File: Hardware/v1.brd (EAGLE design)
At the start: 50 x 40 mm, 75 parts, among them IC1 LM324D, IC2 m328p, IC3 REG1117, J1 22-27-2061-06, J2 22-27-2021-02, J3 22-27-2021-02, J4 22-27-2031-03, J5 22-27-2041-04, Q1 BSS123, Q2 BSS123, Q3 BSS123, Q5 BSS123

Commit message: slight changes in the layout
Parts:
- C9: value (none) -> 1000u
- L1, L2: device rcl:L2012C -> rcl:L2825P
- U$1: device IRF7424:SO-08 -> MyLib:SO-08
- U$3: value ELKO-1,27-4,2 -> 330u; device MyLib:ELKO-1,27-4,5 -> rcl:E2-5
- U$4: value ELKO-1,27-4,2 -> 330u; device MyLib:ELKO-1,27-4,5 -> rcl:E3,5-8
- moved TP12 2.29 mm to (9.08, 35.6), flipped to the bottom
- moved U$4 2.10 mm to (11.2, 35.7)
- moved C5 1.40 mm to (23.0, 2.71), turned to 90 degrees
- moved TP8 1.11 mm to (9.08, 37.8)
- moved L2 0.95 mm to (15.3, 33.8)
- moved U$3 0.94 mm to (2.98, 28.5), turned to 90 degrees
- moved L1 0.59 mm to (19.7, 2.58)
- moved R24 0.51 mm to (12.1, 31.6)
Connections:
- net 12V: now also U$4.+; no longer U$4.P$1
- net GND: now also U$3.-, U$4.-; no longer U$3.P$2, U$4.P$2
- net VCC: now also U$3.+; no longer U$3.P$1
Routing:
- net VCC: track 148.6 -> 145.7 mm
- net N$26: track 5.80 -> 8.57 mm
- net N$5: track 4.79 -> 7.38 mm
- net N$3: track 3.33 -> 5.04 mm
- net 12V: track 82.1 -> 80.8 mm

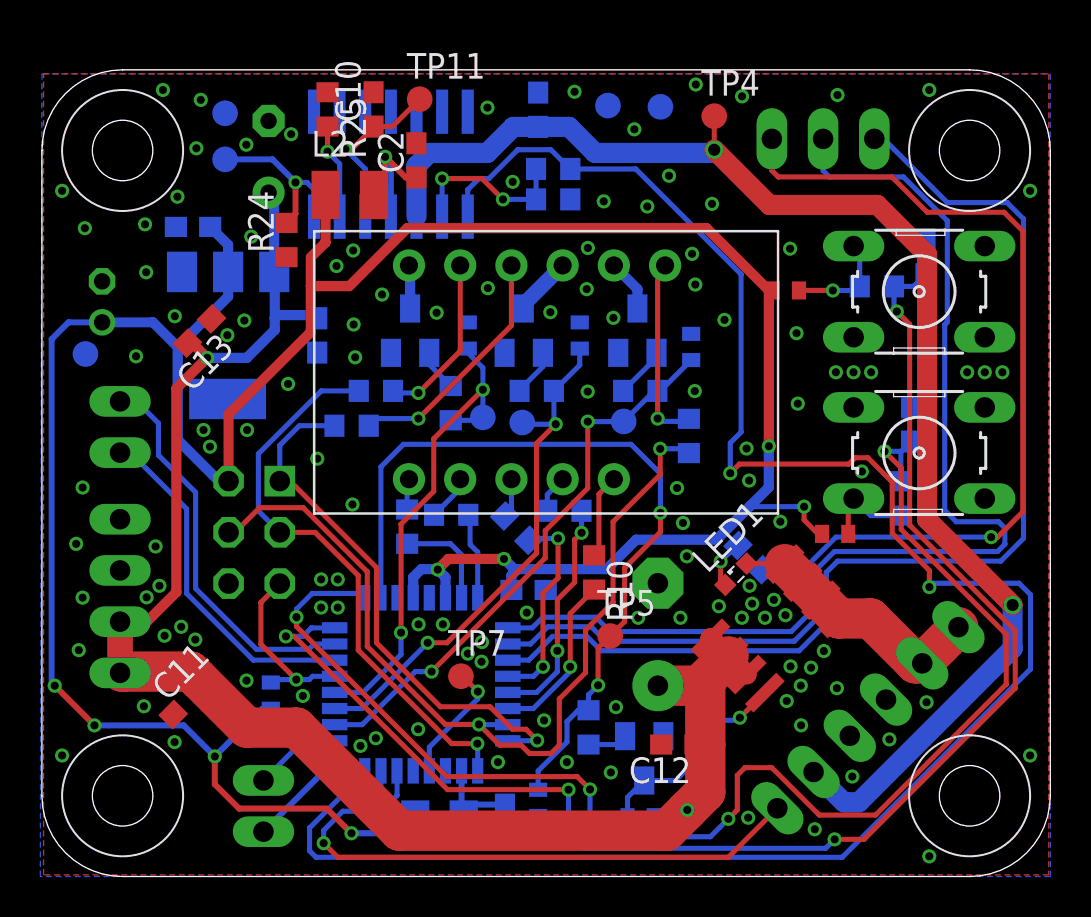
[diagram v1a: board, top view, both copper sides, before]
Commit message: finish layer done so pcb will have the components names printed on it
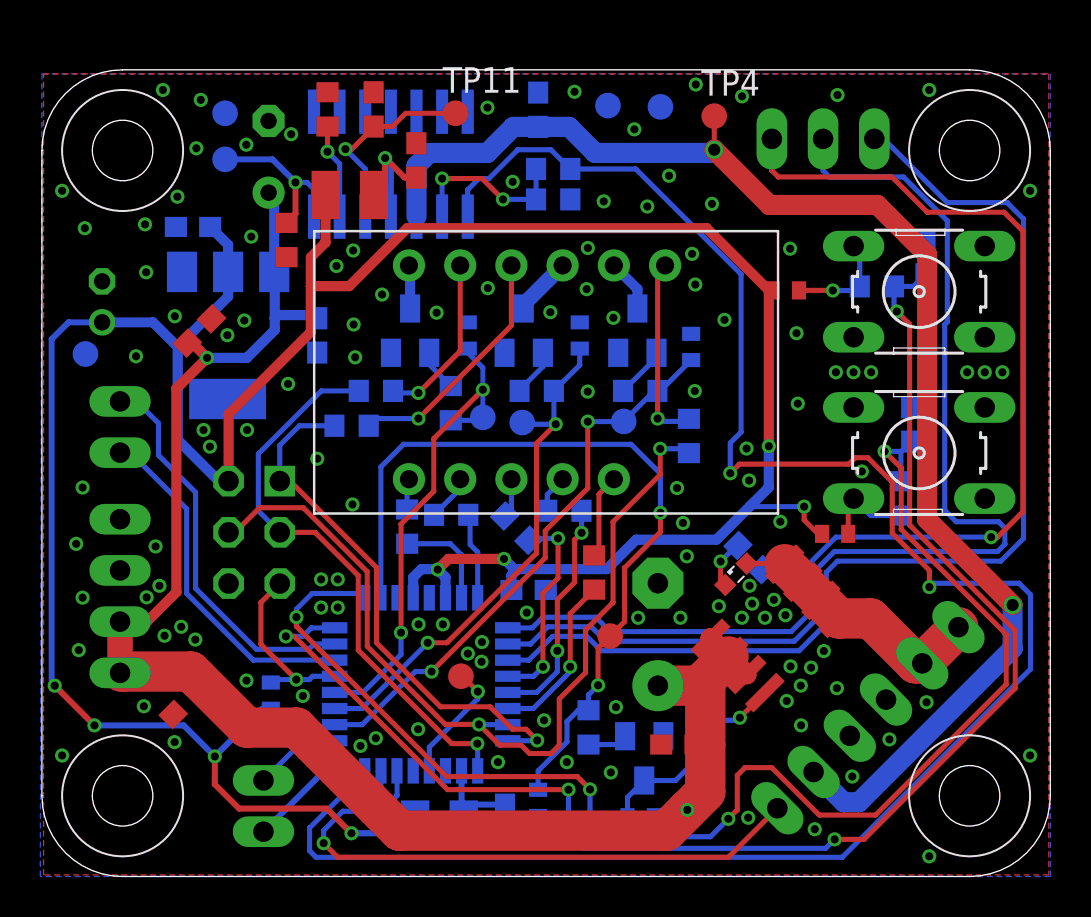
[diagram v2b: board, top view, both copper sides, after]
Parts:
- moved TP11 1.91 mm to (20.5, 37.8)
- renumbered U$3 to C15, U$4 to C14
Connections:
- net N$27 renamed ADC7
- net N$28 renamed ADC1
- net N$29 renamed ADC2
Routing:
- net N$30: track 8.49 -> 9.97 mm
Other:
- board text removed: "ADC6"
- board text removed: "ADC7"
- board text removed: "by JB v1.0 08-2014"

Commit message: op-amp rework
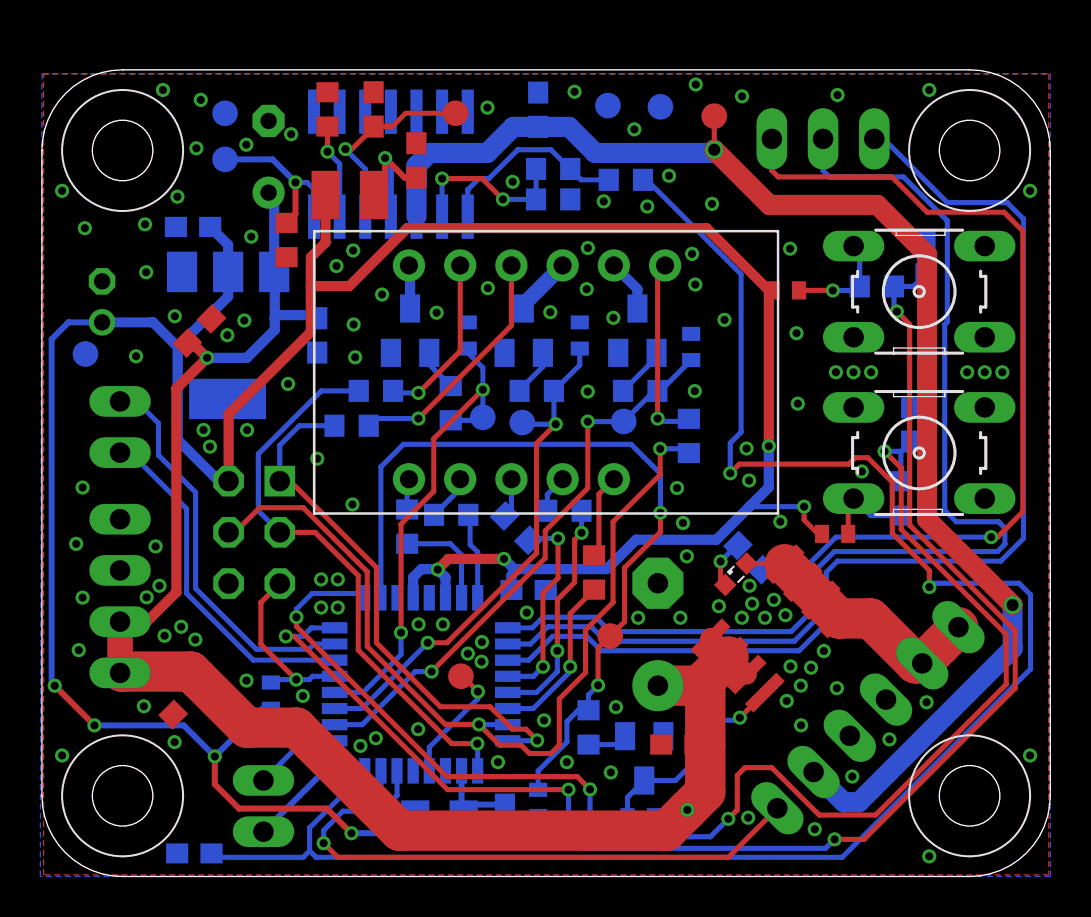
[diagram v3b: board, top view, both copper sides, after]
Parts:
- added C16: 10n, rcl:C0603
- added R27: 5k6, rcl:R0603
- R1: value 750k -> 68k
- R2: value 1k2 -> 100
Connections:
- new net SDFGHJK: IC1.1, R1.2, R27.1
- net ADC0: now also C16.1, R27.2; no longer IC1.1, R1.2
- net GND: now also C16.2
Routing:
- net SDFGHJK: track 0.00 -> 9.76 mm
- net ADC0: track 98.3 -> 91.9 mm
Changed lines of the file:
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@@
 <layer number="23" name="tOrigins" color="15" fill="1" visible="yes" active="yes"/>
 <layer number="24" name="bOrigins" color="15" fill="1" visible="yes" active="yes"/>
-<layer number="25" name="tNames" color="7" fill="1" visible="no" active="yes"/>
-<layer number="26" name="bNames" color="7" fill="1" visible="no" active="yes"/>
-<layer number="27" name="tValues" color="7" fill="1" visible="no" active="yes"/>
-<layer number="28" name="bValues" color="7" fill="1" visible="no" active="yes"/>
+<layer number="25" name="tNames" color="7" fill="1" visible="yes" active="yes"/>
+<layer number="26" name="bNames" color="7" fill="1" visible="yes" active="yes"/>
+<layer number="27" name="tValues" color="7" fill="1" visible="yes" active="yes"/>
+<layer number="28" name="bValues" color="7" fill="1" visible="yes" active="yes"/>
 <layer number="29" name="tStop" color="7" fill="3" visible="yes" active="yes"/>
 <layer number="30" name="bStop" color="7" fill="6" visible="yes" active="yes"/>
@@
 <elements>
 <element name="IC1" library="linear" package="SO14" value="LM324D" x="17.30375" y="35.321875" smashed="yes" rot="MR0"/>
-<element name="R2" library="rcl" package="R0603" value="1k2" x="25.352375" y="33.575625" smashed="yes" rot="MR0">
-<attribute name="NAME" x="26.781125" y="34.178875" size="1.143" layer="34" font="vector" ratio="15" rot="MR180"/>
-</element>
-<element name="R1" library="rcl" package="R0603" value="750k" x="25.352375" y="35.08375" smashed="yes" rot="MR180">
-<attribute name="NAME" x="26.749375" y="35.71875" size="1.143" layer="34" font="vector" ratio="15" rot="MR180"/>
+<element name="R2" library="rcl" package="R0603" value="100" x="25.352375" y="33.575625" smashed="yes" rot="MR0">
+<attribute name="NAME" x="24.114125" y="32.718375" size="1.143" layer="34" font="vector" ratio="15" rot="MR180"/>
+</element>
+<element name="R1" library="rcl" package="R0603" value="68k" x="25.352375" y="35.08375" smashed="yes" rot="MR180">
+<attribute name="NAME" x="26.622375" y="36.41725" size="1.143" layer="34" font="vector" ratio="15" rot="MR180"/>
 </element>
 <element name="C1" library="rcl" package="C0603" value="10n" x="24.60625" y="38.020625" smashed="yes" rot="MR90">
@@
 <attribute name="VALUE" x="29.48305" y="21.802725" size="0.0254" layer="28" rot="MR0"/>
 </element>
-<element name="TP4" library="testpad" package="B1,27" value="PTR1B1,27" x="33.3375" y="37.703125">
-<attribute name="TP_SIGNAL_NAME" value="" x="33.3375" y="37.703125" size="1.778" layer="27" display="off"/>
+<element name="TP4" library="testpad" package="B1,27" value="PTR1B1,27" x="33.3375" y="37.703125" smashed="yes">
+<attribute name="TP_SIGNAL_NAME" value="" x="32.7025" y="35.798125" size="1" layer="37"/>
+<attribute name="VALUE" x="32.7025" y="36.941125" size="0.0254" layer="27"/>
 </element>
 <element name="TP5" library="testpad" package="B1,27" value="PTR1B1,27" x="28.178125" y="11.922125" smashed="yes">
@@
 <attribute name="NAME" x="17.3355" y="38.608" size="1.143" layer="33" font="vector" ratio="15"/>
 </element>
-<element name="TP11" library="testpad" package="B1,27" value="PTR1B1,27" x="20.5105" y="37.846">
-<attribute name="TP_SIGNAL_NAME" value="" x="20.5105" y="37.846" size="1.778" layer="27" display="off"/>
+<element name="TP11" library="testpad" package="B1,27" value="PTR1B1,27" x="20.5105" y="37.846" smashed="yes">
+<attribute name="TP_SIGNAL_NAME" value="" x="19.8755" y="35.941" size="1" layer="37"/>
+<attribute name="VALUE" x="19.8755" y="37.084" size="0.0254" layer="27"/>
 </element>
 <element name="TP12" library="testpad" package="B1,27" value="PTR1B1,27" x="9.0805" y="35.56" smashed="yes" rot="MR0">
@@
 <element name="C14" library="rcl" package="E3,5-8" value="330u" x="11.2395" y="35.687" smashed="yes" rot="MR90">
 <attribute name="NAME" x="12.954" y="35.1155" size="1.143" layer="34" font="vector" ratio="15" rot="MR0"/>
+</element>
+<element name="C16" library="rcl" package="C0603" value="10n" x="7.5565" y="1.143" smashed="yes" rot="MR0">
+<attribute name="NAME" x="8.89" y="2.032" size="1.143" layer="34" font="vector" ratio="15" rot="MR0"/>
+</element>
+<element name="R27" library="rcl" package="R0603" value="5k6" x="28.956" y="34.544" smashed="yes" rot="MR180">
+<attribute name="NAME" x="28.702" y="33.655" size="1.143" layer="34" font="vector" ratio="15" rot="MR180"/>
 </element>
 </elements>
@@
 <via x="13.843" y="14.732" extent="1-16" drill="0.4"/>
 <via x="14.6685" y="14.732" extent="1-16" drill="0.4"/>
+<contactref element="C16" pad="2"/>
 </signal>
 <signal name="N$1">
@@
 <signal name="ADC0">
 <contactref element="IC2" pad="23"/>
-<wire x1="29.448125" y1="35.08375" x2="34.671" y2="29.860875" width="0.254" layer="16"/>
 <wire x1="16.80875" y1="4.346875" x2="16.80875" y2="5.235525" width="0.254" layer="16"/>
-<contactref element="IC1" pad="1"/>
-<contactref element="R1" pad="2"/>
-<wire x1="25.24125" y1="36.03625" x2="26.19375" y2="35.08375" width="0.254" layer="16"/>
-<wire x1="26.19375" y1="35.08375" x2="26.202375" y2="35.08375" width="0.254" layer="16"/>
-<wire x1="29.448125" y1="35.08375" x2="26.202375" y2="35.08375" width="0.254" layer="16"/>
-<wire x1="21.11375" y1="34.051875" x2="21.11375" y2="32.721875" width="0.254" layer="16"/>
 <wire x1="16.80875" y1="4.346875" x2="16.589375" y2="4.1275" width="0.254" layer="16"/>
 <wire x1="16.589375" y1="4.1275" x2="14.986" y2="4.1275" width="0.254" layer="16"/>
@@
 <wire x1="40.005" y1="20.447" x2="34.5821" y2="20.447" width="0.254" layer="1"/>
 <wire x1="44.196" y1="14.5415" x2="44.0055" y2="14.351" width="0.254" layer="16"/>
-<wire x1="21.11375" y1="34.051875" x2="21.669375" y2="34.6075" width="0.254" layer="16"/>
-<wire x1="21.669375" y1="34.6075" x2="22.1615" y2="34.6075" width="0.254" layer="16"/>
-<wire x1="22.1615" y1="34.6075" x2="23.59025" y2="36.03625" width="0.254" layer="16"/>
-<wire x1="23.59025" y1="36.03625" x2="25.24125" y2="36.03625" width="0.254" layer="16"/>
+<contactref element="C16" pad="1"/>
+<contactref element="R27" pad="2"/>
+<wire x1="34.671" y1="29.860875" x2="29.987875" y2="34.544" width="0.25" layer="16"/>
+<wire x1="29.987875" y1="34.544" x2="29.806" y2="34.544" width="0.25" layer="16"/>
+<wire x1="8.4065" y1="1.143" x2="8.509" y2="1.143" width="0.25" layer="16"/>
+<wire x1="8.509" y1="1.143" x2="8.6995" y2="0.9525" width="0.25" layer="16"/>
+<wire x1="8.6995" y1="0.9525" x2="12.954" y2="0.9525" width="0.25" layer="16"/>
+<wire x1="12.954" y1="0.9525" x2="13.2715" y2="1.27" width="0.25" layer="16"/>
 </signal>
 <signal name="SENSOR0">
@@
 <wire x1="18.034" y1="37.846" x2="17.3745" y2="37.1865" width="0.25" layer="1"/>
 </signal>
+<signal name="SDFGHJK">
+<contactref element="IC1" pad="1"/>
+<contactref element="R1" pad="2"/>
+<contactref element="R27" pad="1"/>
+<wire x1="25.24125" y1="36.03625" x2="26.19375" y2="35.08375" width="0.254" layer="16"/>
+<wire x1="26.19375" y1="35.08375" x2="26.202375" y2="35.08375" width="0.254" layer="16"/>
+<wire x1="21.11375" y1="34.051875" x2="21.11375" y2="32.721875" width="0.254" layer="16"/>
+<wire x1="21.11375" y1="34.051875" x2="21.669375" y2="34.6075" width="0.254" layer="16"/>
+<wire x1="21.669375" y1="34.6075" x2="22.1615" y2="34.6075" width="0.254" layer="16"/>
+<wire x1="22.1615" y1="34.6075" x2="23.59025" y2="36.03625" width="0.254" layer="16"/>
+<wire x1="23.59025" y1="36.03625" x2="25.24125" y2="36.03625" width="0.254" layer="16"/>
+<wire x1="26.202375" y1="35.08375" x2="26.742125" y2="34.544" width="0.25" layer="16"/>
+<wire x1="26.742125" y1="34.544" x2="28.106" y2="34.544" width="0.25" layer="16"/>
+</signal>
 </signals>

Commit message: latest version with some updates
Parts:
- added AREF: PTR1B1,27, testpad:B1,27
- R1: value 68k -> 43k
- moved TP7 9.94 mm to (11.4, 6.73), flipped to the bottom
- moved R15 0.54 mm to (33.1, 7.28)
- moved TP4 0.51 mm to (32.8, 37.8)
- moved C6 0.45 mm to (7.81, 31.9)
- moved C12 0.06 mm to (31.6, 6.54)
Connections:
- net ADC0 renamed THERMO0
- net ADC1 renamed HALL
- removed net N$24: IC2.20, TP7.TP
- new net AREF: AREF.TP, IC2.20
- net ADC2: now also TP7.TP; no longer J3.2
- net VCC: now also J3.2
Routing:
- net GND: track 0.00 -> 7.48 mm
- net N$24: track 6.08 -> 0.00 mm, vias 1 -> 0
- net AREF: track 0.00 -> 6.08 mm, vias 0 -> 1
- net 12V: track 80.8 -> 79.5 mm
- net ADC2: track 4.34 -> 3.15 mm
- net N$32: track 5.53 -> 6.07 mm
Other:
- board text added: "1"
- board text added: "H"
- board text added: "V"
- board text removed: "PC1"
- board text removed: "PC2"

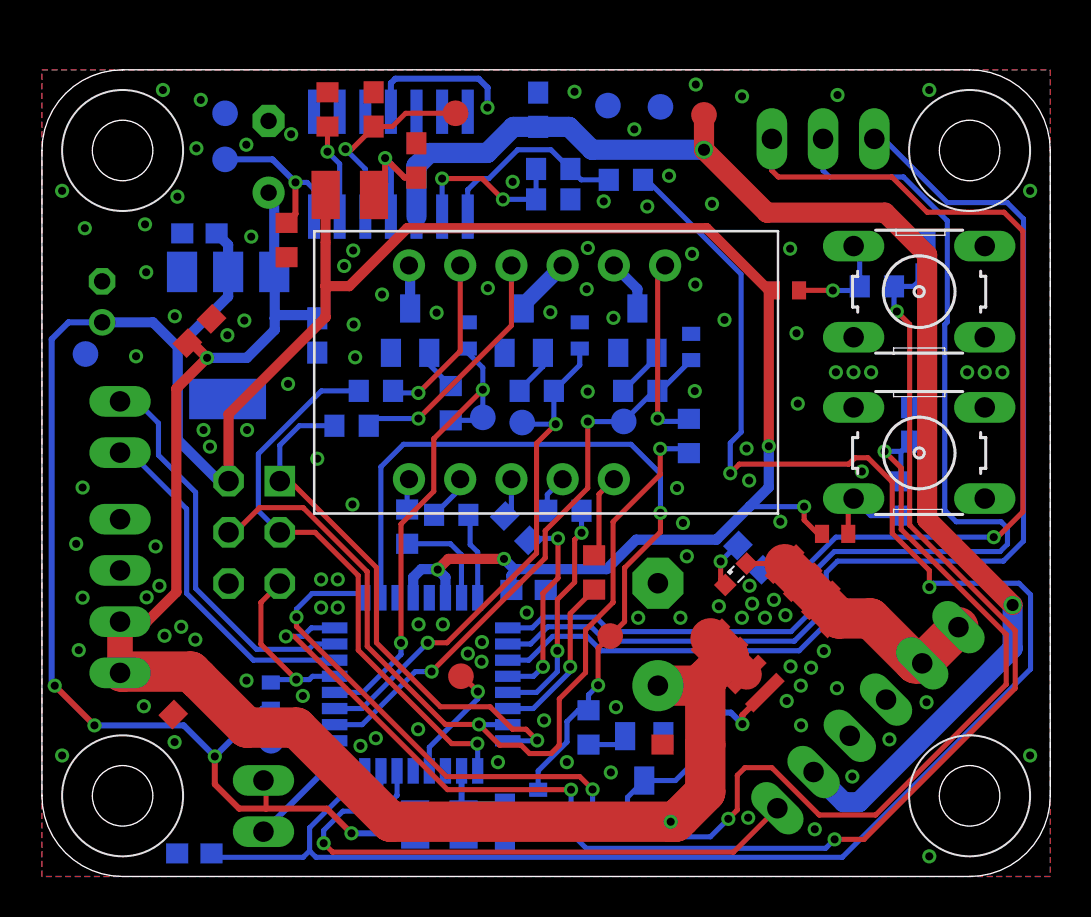
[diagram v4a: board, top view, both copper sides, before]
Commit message: some resistor sizes changed from 0402 to 0603
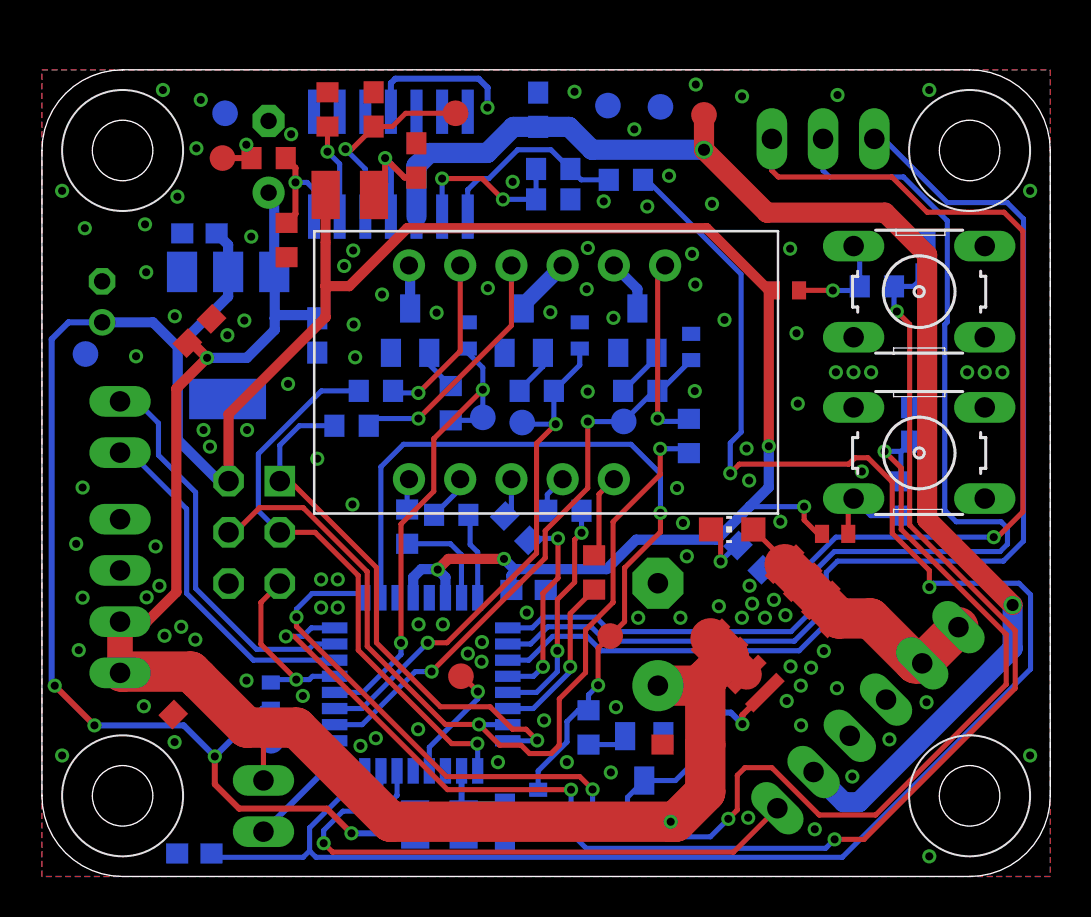
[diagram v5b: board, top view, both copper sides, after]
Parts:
- added R28: n.m., rcl:R0603
- C10: value 10n -> n.m.
- LED1: device eagle-ltspice:LED_SML0603 -> led:CHIP-LED0805
- R10, R11, R12, R13, R14, R3, R4, R8: value 330 -> 150
- R22, R23: value 160k -> 10k
- R24: value 750k -> n.m.
- R25: value 1k2 -> n.m.
- R26: value 100 -> 1k
- moved LED1 2.23 mm to (34.2, 17.2), turned to 90 degrees
- moved TP12 0.14 mm to (8.95, 35.6), flipped to the top
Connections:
- new net N$21: R28.1, TP12.TP
- net 12V: now also J3.2
- net N$26: now also R28.2; no longer TP12.TP
- net VCC: no longer J3.2
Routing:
- net 12V: track 79.5 -> 82.4 mm
- net N$26: track 8.57 -> 6.01 mm
- net VCC: track 146.0 -> 144.6 mm
- net N$21: track 0.00 -> 1.44 mm
- net N$25: track 2.45 -> 2.97 mm

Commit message: finalized
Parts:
- R18, R19, R36, R37, R5, R6, R7, R9: device rcl:R0402 -> rcl:R0603
- R27: value 5k6 -> 10k
- moved R19 1.02 mm to (37.9, 29.1)
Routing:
- net N$23: track 5.22 -> 4.00 mm
- net VCC: track 144.6 -> 145.1 mm
